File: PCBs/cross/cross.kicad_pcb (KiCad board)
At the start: 2 copper layers, 111 x 98 mm, 14 parts, among them J1 PWR_Conn, U1 ctrlr_TL, U2 LEDs_T, U3 ctrlr_BR, U4 LEDs_B, U5 LEDs_R, U6 LEDs_L, U7 ctrlr_C, U8 ESP32-C6-DEVKITC-1-N8, U9 LEDs_C

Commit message: Split PCB in two : cross + logic
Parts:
- removed J1: PWR_Conn, Connector_BarrelJack:BarrelJack_Horizontal
- removed U8: ESP32-C6-DEVKITC-1-N8, ESP32-C6-DEVKITC-1-N8:MODULE_ESP32-C6-DEVKITC-1-N8
- added J2: Conn_01x04, Connector_PinHeader_2.54mm:PinHeader_1x04_P2.54mm_Vertical, B.Cu at (203.5, 89.1)
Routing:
- net GND: track 0.00 -> 0.66 mm
- net /SDA: track 0.00 -> 0.50 mm
- net /SCL: track 0.00 -> 0.50 mm
- net +5V: track 0.00 -> 0.50 mm
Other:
- board size 111 x 98 mm -> 122.5 x 110 mm

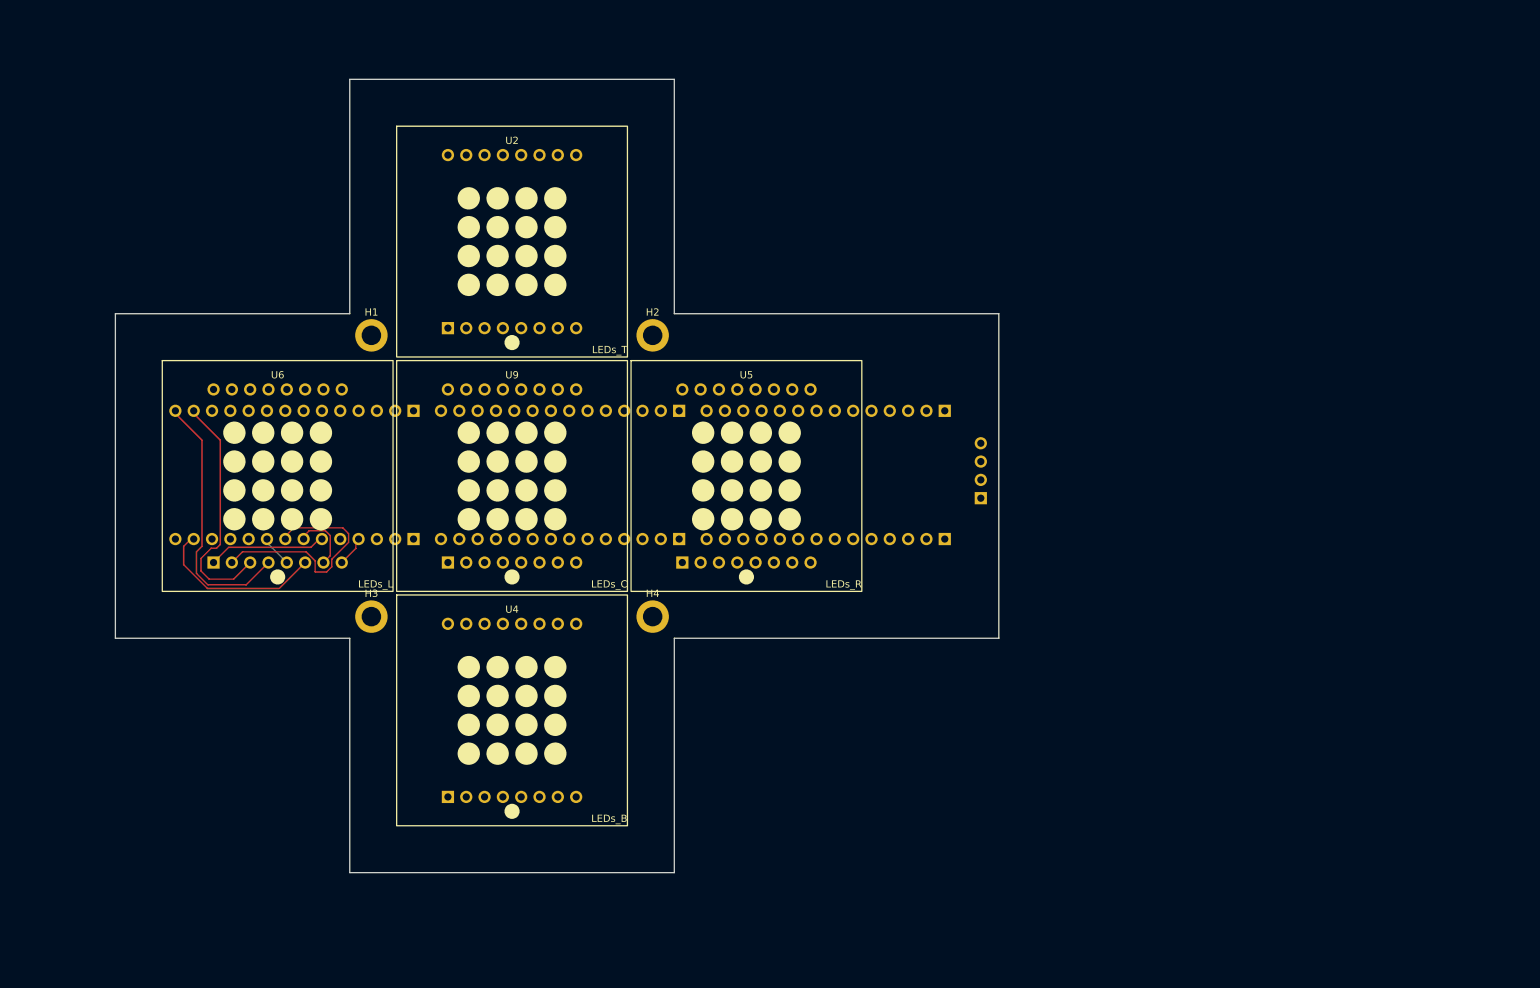
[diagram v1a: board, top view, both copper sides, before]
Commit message: Cross routing 1/3 done
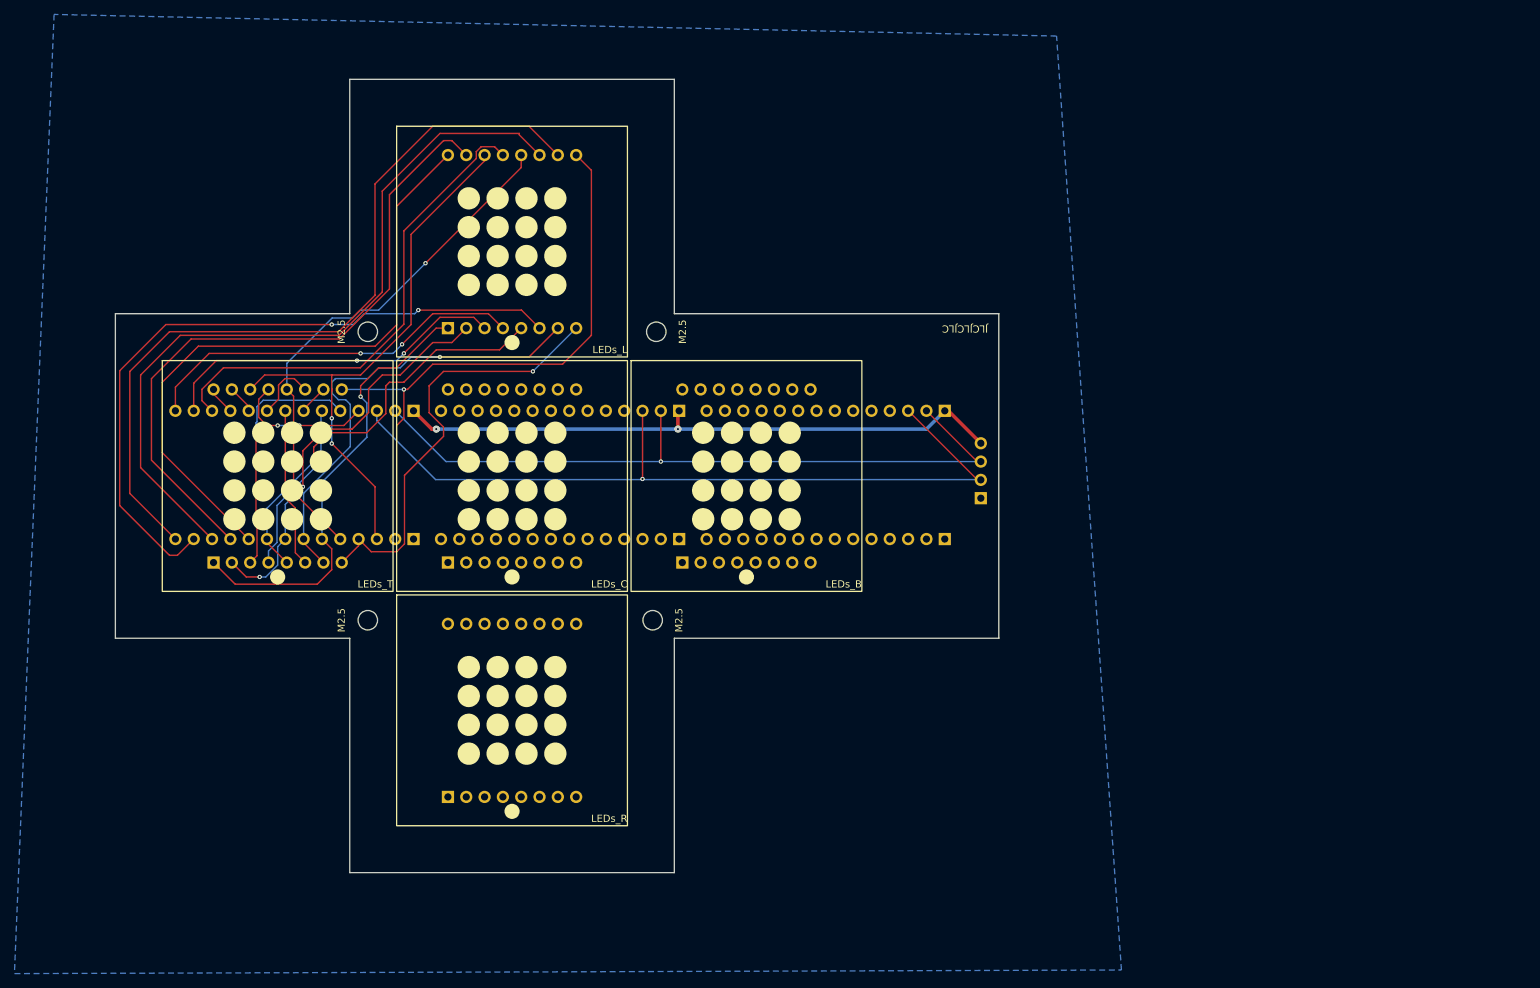
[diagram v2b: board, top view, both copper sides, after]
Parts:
- H1, H2, H3, H4: value MountingHole_Pad -> M2.5; footprint MountingHole:MountingHole_2.7mm_M2.5_ISO7380_Pad -> MountingHole:MountingHole_2.7mm_M2.5
- J2: value Conn_01x04 -> Interconnect
- moved U2 46.0 mm to (106.0, 86.0)
- moved U4 46.0 mm to (171.0, 86.0)
- moved U5 46.0 mm to (138.5, 118.5)
- moved U6 46.0 mm to (138.5, 53.5)
- moved H1 0.71 mm to (118.5, 66.0), turned to -90 degrees
- moved H2 0.71 mm to (158.5, 66.0), turned to 90 degrees
- moved H3 0.71 mm to (118.5, 106.0), turned to -90 degrees
- moved H4 0.50 mm to (158.0, 106.0), turned to 90 degrees
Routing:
- net /SCL: track 0.50 -> 112.1 mm, vias 0 -> 1
- net Net-(U1-A11): track 0.00 -> 110.0 mm
- net Net-(U1-A13): track 0.00 -> 105.6 mm
- net /SDA: track 0.50 -> 101.6 mm, vias 0 -> 1
- net Net-(U1-A14): track 0.00 -> 92.6 mm
- net Net-(U1-A15): track 0.00 -> 89.0 mm
- net Net-(U1-C0): track 0.00 -> 84.8 mm, vias 0 -> 1
- net +5V: track 0.50 -> 85.2 mm, vias 0 -> 2
- net Net-(U1-C1): track 0.00 -> 79.3 mm, vias 0 -> 2
- net Net-(U1-C3): track 0.00 -> 72.9 mm, vias 0 -> 1
- net Net-(U1-A12): track 23.7 -> 95.5 mm, vias 0 -> 2
- net Net-(U1-A8): track 0.00 -> 67.8 mm
- net Net-(U1-C2): track 4.07 -> 60.5 mm, vias 0 -> 1
- net Net-(U1-C5): track 8.95 -> 64.9 mm, vias 0 -> 1
- net Net-(U1-C7): track 4.55 -> 57.7 mm, vias 0 -> 1
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- added copper zone on B.Cu, net GND
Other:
- board text added: "JLCJLCJLC"

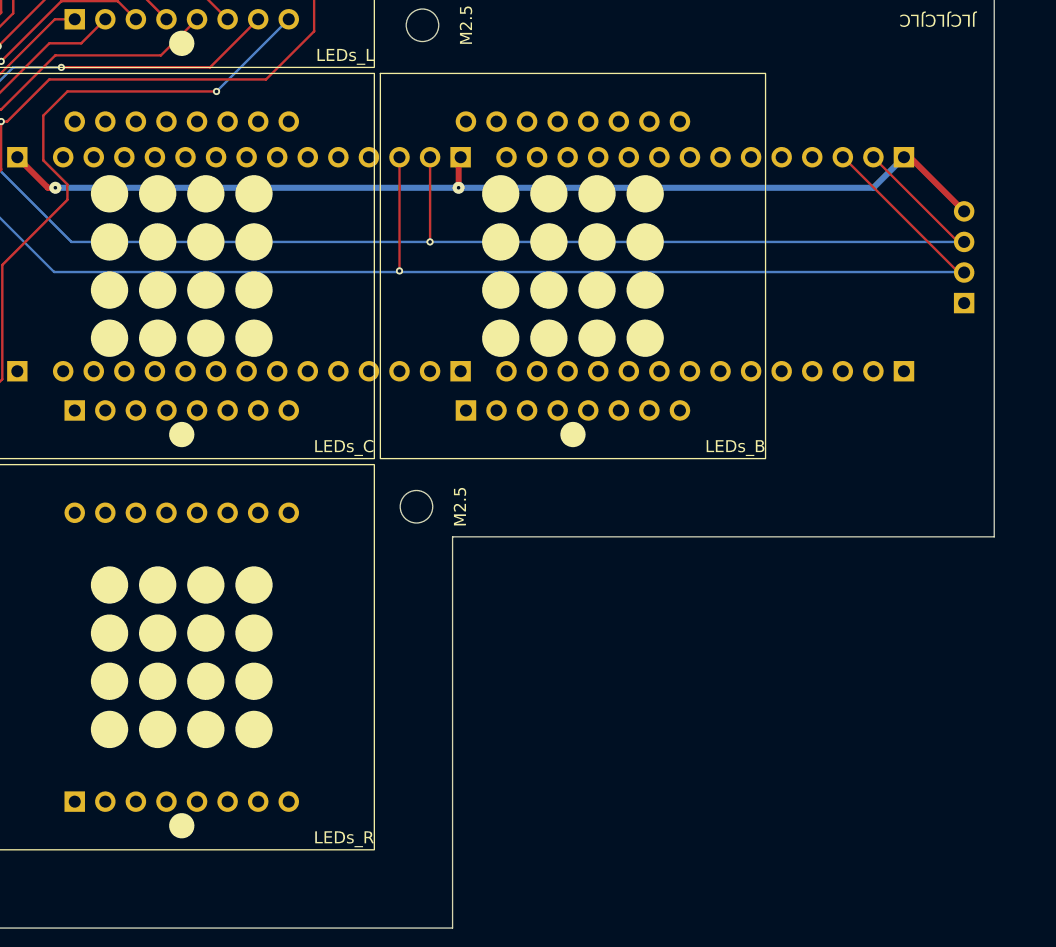
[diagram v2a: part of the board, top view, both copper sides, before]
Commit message: Cross routing 2/3 done
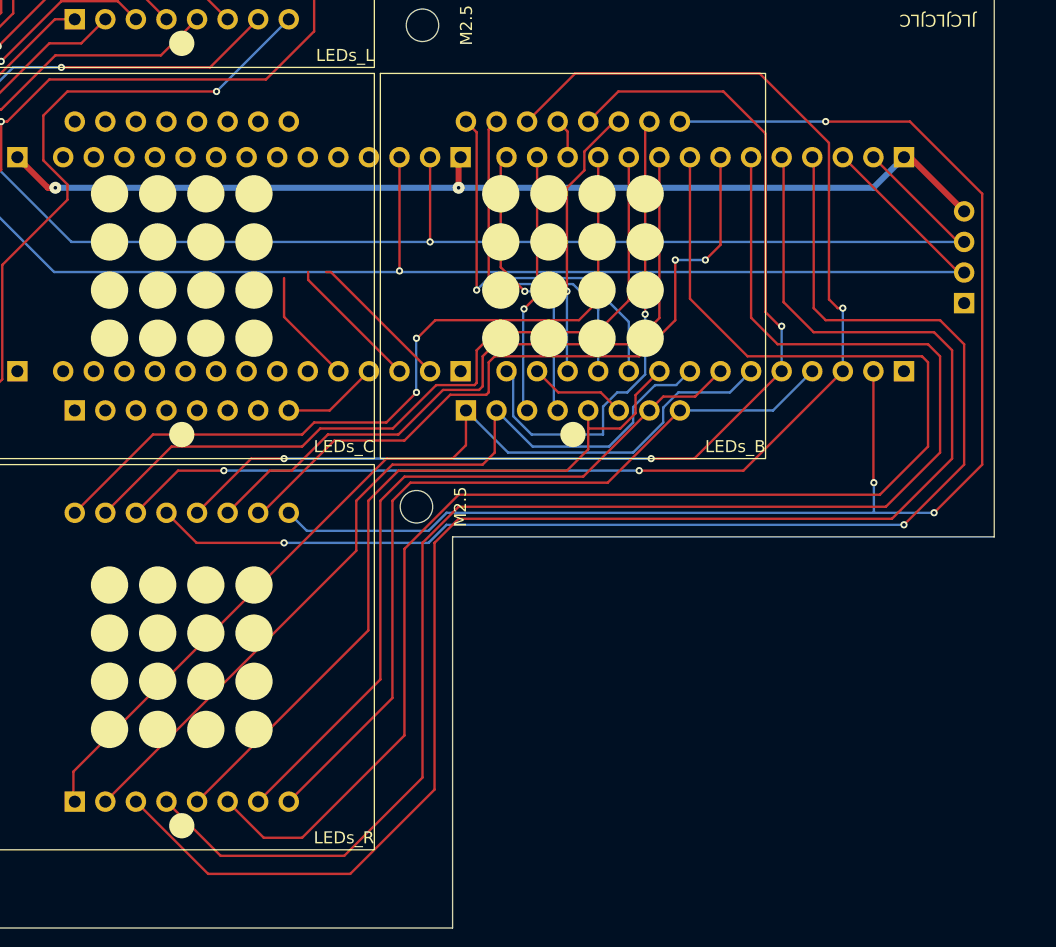
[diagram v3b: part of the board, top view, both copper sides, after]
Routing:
- net Net-(U3-A1): track 0.00 -> 133.4 mm
- net Net-(U3-A2): track 0.00 -> 129.8 mm
- net Net-(U3-A4): track 0.00 -> 122.7 mm
- net Net-(U3-C0): track 0.00 -> 122.4 mm, vias 0 -> 3
- net Net-(U3-C1): track 0.00 -> 112.4 mm, vias 0 -> 3
- net Net-(U3-A0): track 0.00 -> 106.3 mm, vias 0 -> 2
- net Net-(U3-C3): track 0.00 -> 91.1 mm, vias 0 -> 3
- net Net-(U3-C4): track 0.00 -> 77.9 mm
- net Net-(U3-C6): track 0.00 -> 71.0 mm
- net Net-(U3-C2): track 0.00 -> 67.9 mm
- net Net-(U3-A7): track 0.00 -> 65.4 mm, vias 0 -> 2
- net Net-(U3-A6): track 0.00 -> 64.3 mm
- net Net-(U3-C7): track 0.00 -> 62.9 mm
- net Net-(U3-C5): track 0.00 -> 61.9 mm
- net Net-(U3-A3): track 0.00 -> 59.3 mm, vias 0 -> 2
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
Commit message: Finished PCBs, ready to order
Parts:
- added G***: LOGO, LOGO, B.Cu at (138.5, 51.5)
- added G***: LOGO, LOGO, B.Cu at (138.5, 114.5)
- U1: value ctrlr_TL -> ctrlr_TR
- U3: value ctrlr_BR -> ctrlr_BL
- moved U5 65.0 mm to (138.5, 53.5)
- moved U6 65.0 mm to (138.5, 118.5)
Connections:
- U5 pad 1: Net-(U3-C4) -> Net-(U1-C4)
- U5 pad 10: Net-(U3-A3) -> Net-(U1-A11)
- U5 pad 11: Net-(U3-A5) -> Net-(U1-A13)
- U5 pad 12: Net-(U3-C3) -> Net-(U1-C3)
- U5 pad 13: Net-(U3-A0) -> Net-(U1-A8)
- U5 pad 14: Net-(U3-C1) -> Net-(U1-C1)
- U5 pad 15: Net-(U3-A6) -> Net-(U1-A14)
- U5 pad 16: Net-(U3-A7) -> Net-(U1-A15)
- U5 pad 2: Net-(U3-C6) -> Net-(U1-C6)
- U5 pad 3: Net-(U3-A1) -> Net-(U1-A9)
- U5 pad 4: Net-(U3-A2) -> Net-(U1-A10)
- U5 pad 5: Net-(U3-C7) -> Net-(U1-C7)
- U5 pad 6: Net-(U3-A4) -> Net-(U1-A12)
- U5 pad 7: Net-(U3-C5) -> Net-(U1-C5)
- U5 pad 8: Net-(U3-C2) -> Net-(U1-C2)
- U5 pad 9: Net-(U3-C0) -> Net-(U1-C0)
- U6 pad 1: Net-(U1-C4) -> Net-(U3-C4)
- U6 pad 10: Net-(U1-A11) -> Net-(U3-A3)
- U6 pad 11: Net-(U1-A13) -> Net-(U3-A5)
- U6 pad 12: Net-(U1-C3) -> Net-(U3-C3)
- U6 pad 13: Net-(U1-A8) -> Net-(U3-A0)
- U6 pad 14: Net-(U1-C1) -> Net-(U3-C1)
- U6 pad 15: Net-(U1-A14) -> Net-(U3-A6)
- U6 pad 16: Net-(U1-A15) -> Net-(U3-A7)
- U6 pad 2: Net-(U1-C6) -> Net-(U3-C6)
- U6 pad 3: Net-(U1-A9) -> Net-(U3-A1)
- U6 pad 4: Net-(U1-A10) -> Net-(U3-A2)
- U6 pad 5: Net-(U1-C7) -> Net-(U3-C7)
- U6 pad 6: Net-(U1-A12) -> Net-(U3-A4)
- U6 pad 7: Net-(U1-C5) -> Net-(U3-C5)
- U6 pad 8: Net-(U1-C2) -> Net-(U3-C2)
- U6 pad 9: Net-(U1-C0) -> Net-(U3-C0)
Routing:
- net Net-(U7-A1): track 0.00 -> 35.9 mm, vias 0 -> 2
- net Net-(U7-A2): track 0.00 -> 31.8 mm, vias 0 -> 2
- net Net-(U7-C1): track 11.4 -> 39.1 mm
- net Net-(U7-C4): track 0.00 -> 23.2 mm
- net Net-(U7-A4): track 0.00 -> 22.0 mm, vias 0 -> 1
- net Net-(U7-C3): track 9.61 -> 31.0 mm, vias 0 -> 2
- net Net-(U7-A0): track 0.00 -> 19.8 mm
- net GND: track 0.66 -> 19.8 mm, vias 0 -> 12
- net Net-(U7-C6): track 0.00 -> 16.3 mm
- net Net-(U7-C0): track 12.0 -> 27.2 mm
- net Net-(U7-A6): track 0.00 -> 10.0 mm
- net Net-(U7-A7): track 0.00 -> 7.89 mm
- net Net-(U7-C5): track 0.00 -> 3.91 mm
- net Net-(U7-C7): track 0.00 -> 3.91 mm
- net Net-(U7-A3): track 0.00 -> 3.62 mm
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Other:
- outline, holes or cut-outs redrawn
- board text added: "Cross PCB V1.0 By Vincent Philippoz 03/2026"
- board text added: "PHARMACY CROSS PROJECT"
